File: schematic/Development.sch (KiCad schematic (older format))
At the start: 17 parts

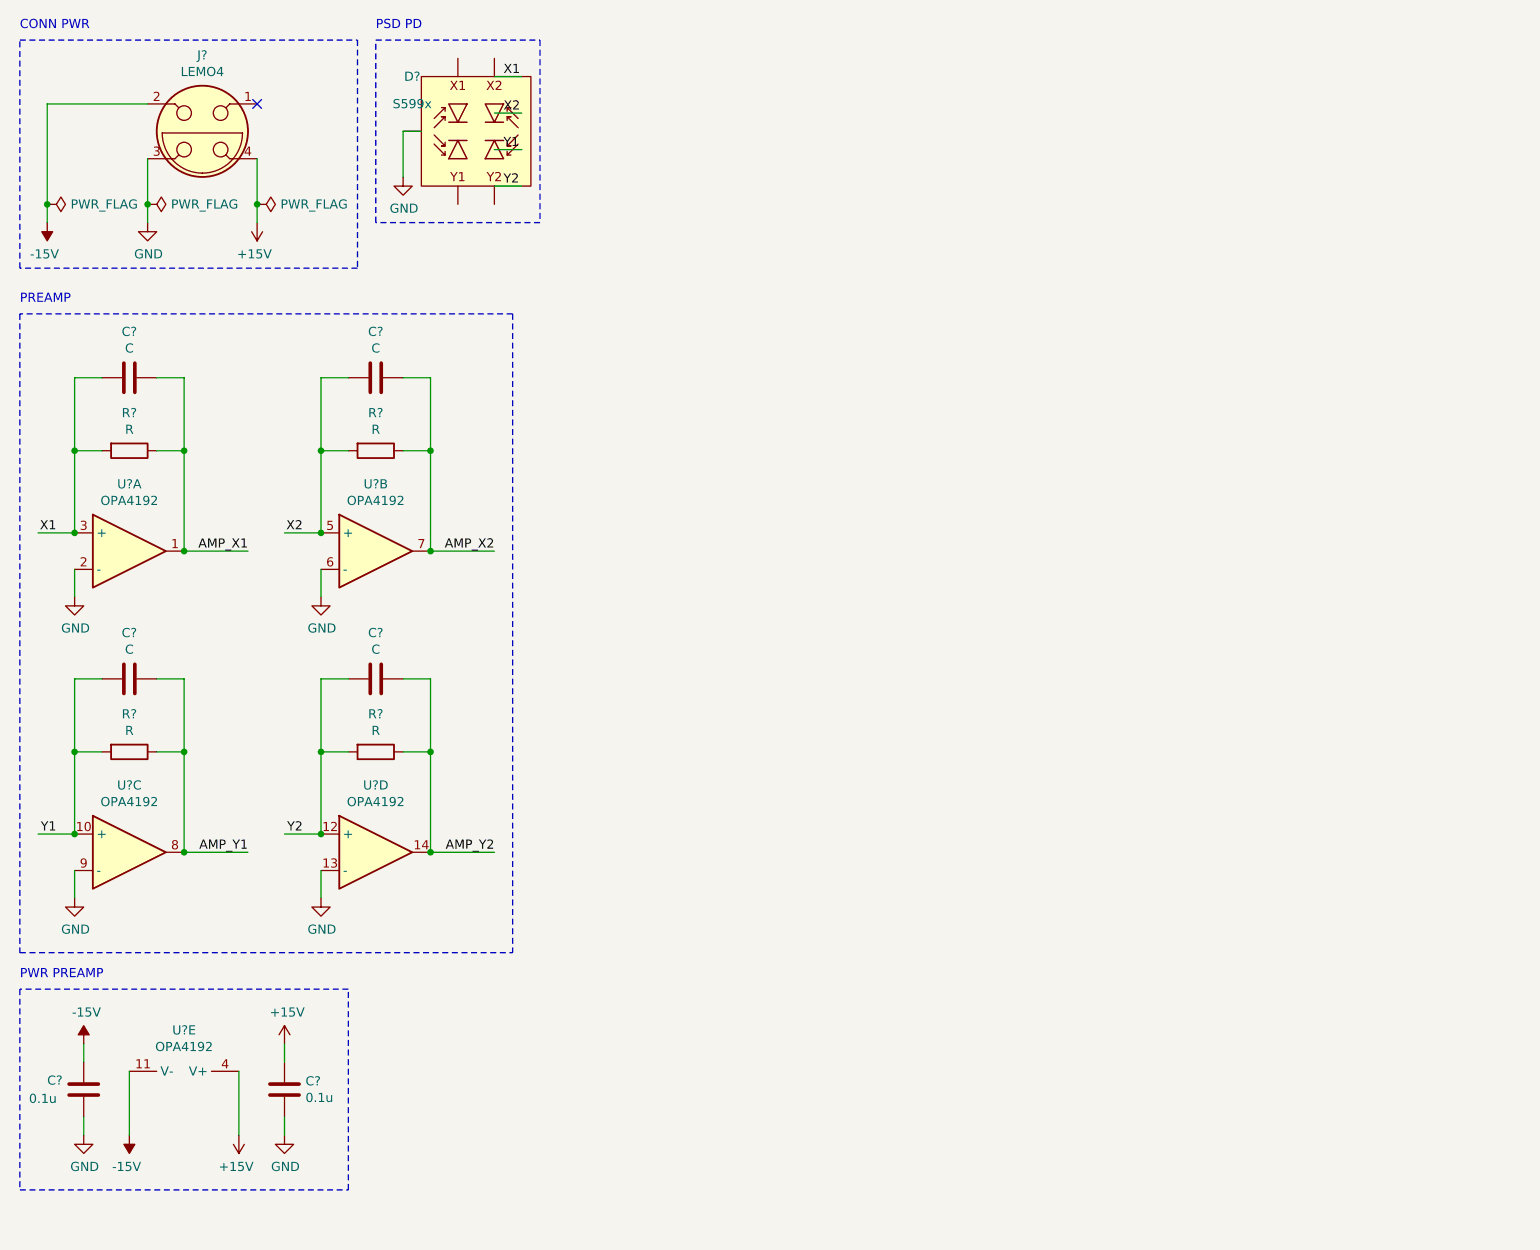
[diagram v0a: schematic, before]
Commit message: added voltage regulator to schematic
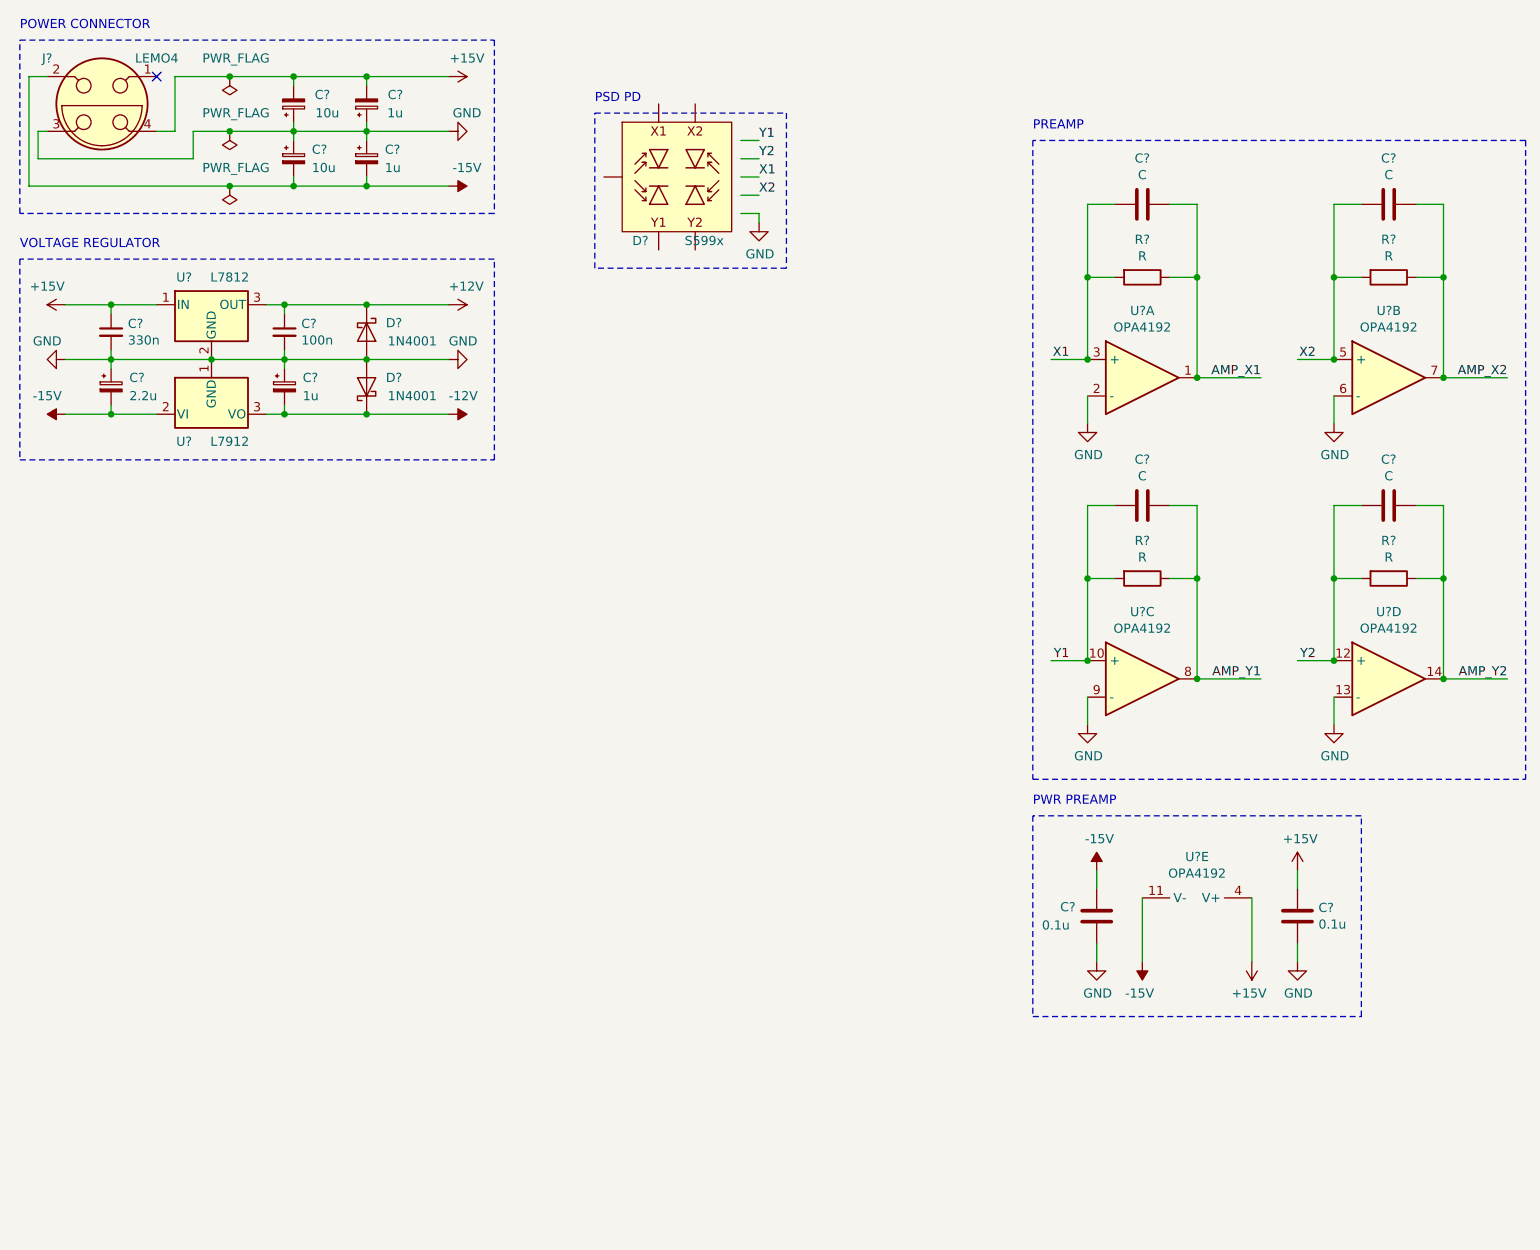
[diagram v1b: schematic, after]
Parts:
- added C? (x2): 10u, symbol Device:CP_Small
- added C? (x3): 1u, symbol Device:CP_Small
- added C?: 330n, symbol Device:C_Small
- added C?: 2.2u, symbol Device:CP_Small
- added C?: 100n, symbol Device:C_Small
- added D? (x2): 1N4001, symbol Device:D_Schottky
- added U?: L7812, symbol Regulator_Linear:L7812
- added U?: L7912, symbol Regulator_Linear:L7912
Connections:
- net labels added: +12V, -12V
- wire segments 63 -> 107
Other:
- note added: "POWER CONNECTOR"
- note added: "VOLTAGE REGULATOR"
- note removed: "CONN PWR"
- moved on the sheet: C?, D?, J?, R?, U?A, U?B, U?C, U?D, U?E

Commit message: redesigned psd + preamp block in schematic
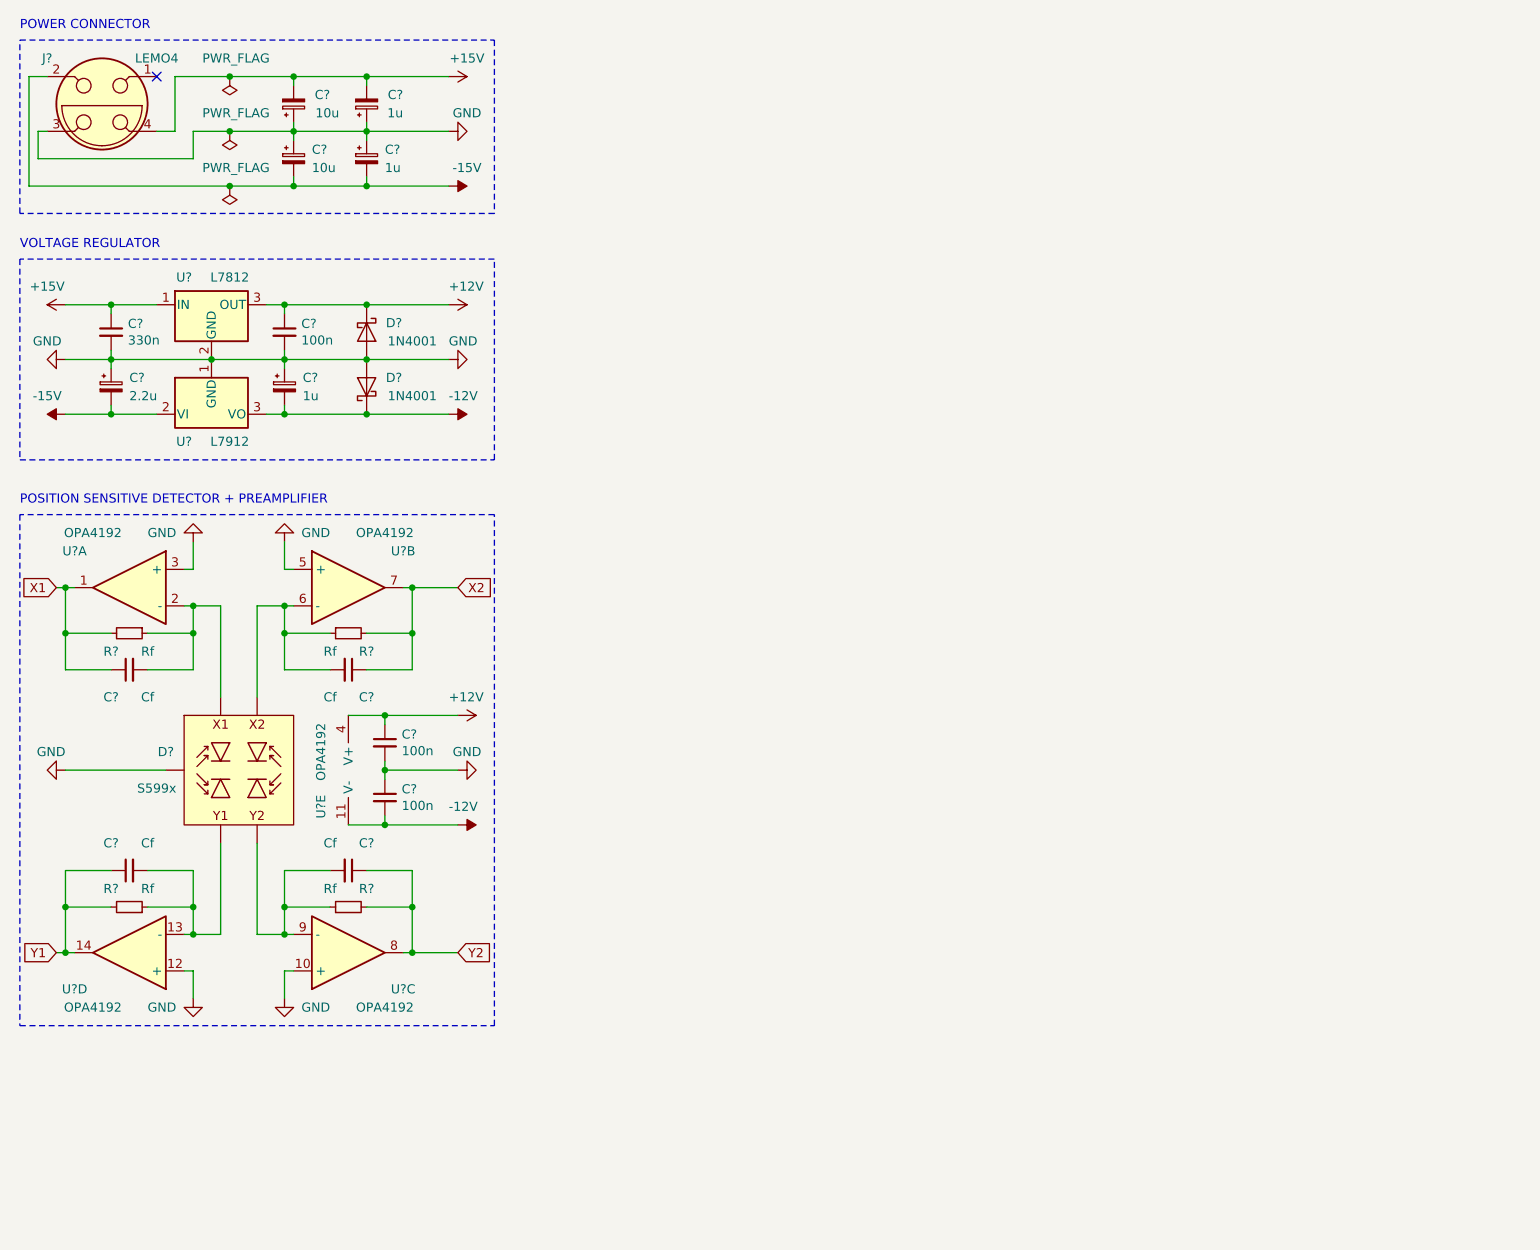
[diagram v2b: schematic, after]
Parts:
- removed C? (x2): 0.1u, symbol Device:C
- removed C? (x4): C, symbol Device:C
- removed R? (x4): R, symbol Device:R
- added C? (x4): Cf, symbol Device:C_Small
- added C? (x2): 100n, symbol Device:C_Small
- added R? (x4): Rf, symbol Device:R_Small
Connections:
- net labels removed: AMP_X1, AMP_X2, AMP_Y1, AMP_Y2
- wire segments 107 -> 121
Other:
- note added: "POSITION SENSITIVE DETECTOR + PREAMPLIFIER"
- note removed: "PREAMP"
- note removed: "PSD PD"
- note removed: "PWR PREAMP"
- moved on the sheet: D?, U?A, U?B, U?C, U?D, U?E

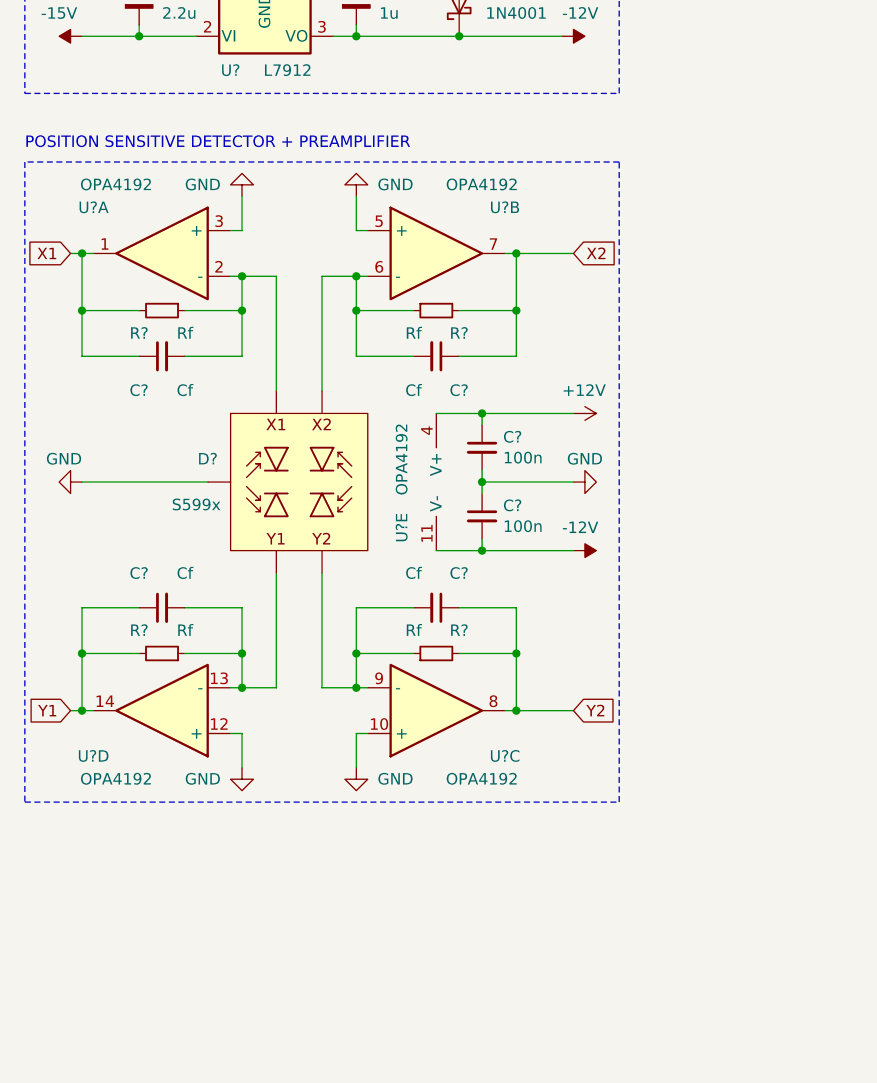
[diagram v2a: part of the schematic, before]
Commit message: added optional offset compensation to preamplifiers
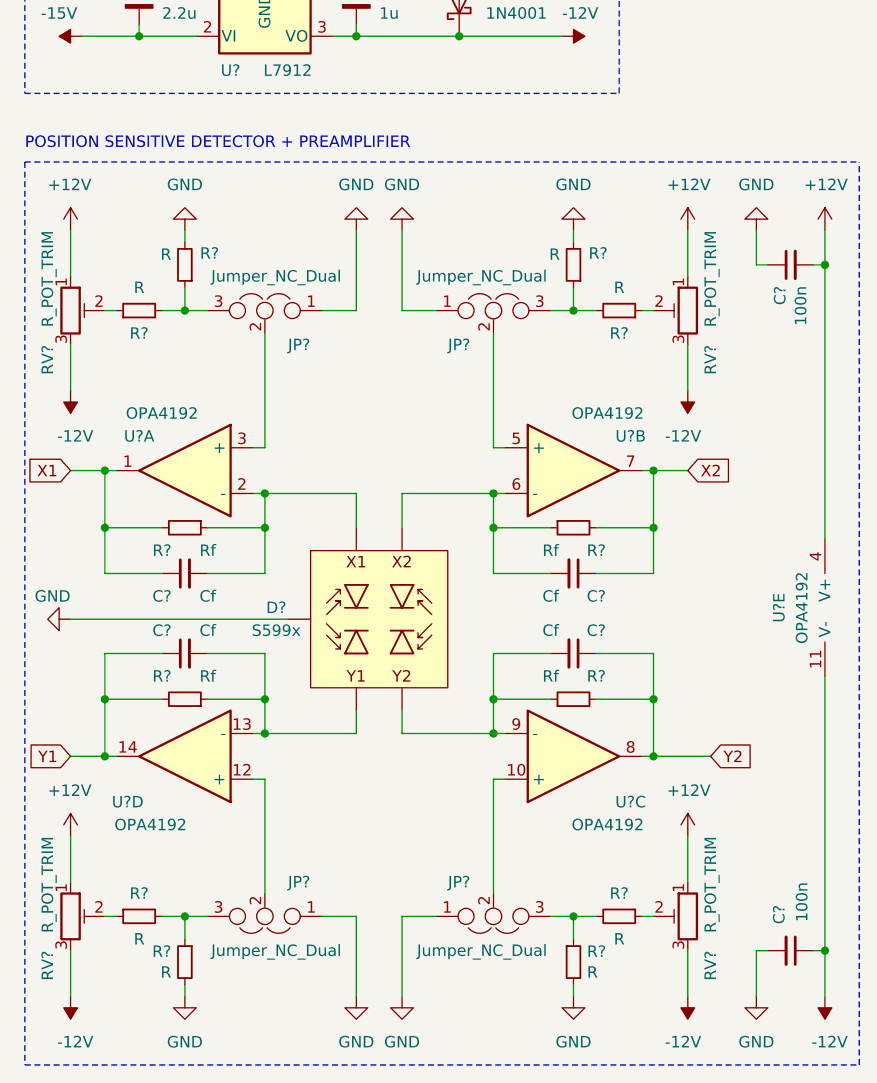
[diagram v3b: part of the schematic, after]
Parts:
- added JP? (x4): Jumper_NC_Dual, symbol Device:Jumper_NC_Dual
- added R? (x8): R, symbol Device:R_Small
- added RV? (x4): R_POT_TRIM, symbol Device:R_POT_TRIM
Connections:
- net +12V: now also C?.2, RV?.1, RV?.1, RV?.1, RV?.1; no longer C?.1
- net -12V: now also C?.1, RV?.3, RV?.3, RV?.3, RV?.3; no longer C?.2
- net GND: now also C?.1, C?.2, JP?.1, JP?.1, JP?.1, JP?.1, R?.2, R?.2, R?.2, R?.2; no longer C?.1, C?.2, U?.10 (+), U?.12 (+), U?.3 (+), U?.5 (+)
- new net: JP?.2, U?.3 (+)
- new net: JP?.2, U?.5 (+)
- new net: JP?.2, U?.10 (+)
- new net: JP?.2, U?.12 (+)
- new net: JP?.3, R?.1, R?.2 (x4)
- new net: R?.1, RV?.2 (x4)
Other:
- moved on the sheet: C?, D?, R?, U?A, U?B, U?C, U?D, U?E
